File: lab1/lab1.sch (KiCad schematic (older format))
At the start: 15 parts

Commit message: Finish 1.8-1.10
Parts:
- added J?: Conn_01x06_Male, symbol Connector:Conn_01x06_Male
- added J?: USB_OTG, symbol Connector:USB_OTG
- added U?: LM1117ADJ, symbol lab1:LM1117ADJ
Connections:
- net +3V3: now also J?.1 (Pin_1)
- net GND: now also J?.3 (Pin_3), J?.5 (GND), J?.6 (Shield)
- new net: J?.1 (VBUS), U?.3 (Vin)
- new net NRST: J?.5 (Pin_5)
- new net PA13: J?.4 (Pin_4)
- new net PA14: J?.2 (Pin_2)
- new net PB3: J?.6 (Pin_6)
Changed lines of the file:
@@
 	4850 4400 4350 4400
 Connection ~ 4350 4400
+$Comp
+L Connector:Conn_01x06_Male J?
+U 1 1 5E299ECA
+P 8650 1750
+F 0 "J?" H 8758 2131 50  0000 C CNN
+F 1 "Conn_01x06_Male" H 8758 2040 50  0000 C CNN
+F 2 "" H 8650 1750 50  0001 C CNN
+F 3 "~" H 8650 1750 50  0001 C CNN
+	1    8650 1750
+	1    0    0    -1
+$EndComp
+Text Label 9500 1950 0    50   ~ 0
+NRST
+$Comp
+L power:+3.3V #PWR?
+U 1 1 5E29CFF8
+P 9500 1550
+F 0 "#PWR?" H 9500 1400 50  0001 C CNN
+F 1 "+3.3V" H 9515 1723 50  0000 C CNN
+F 2 "" H 9500 1550 50  0001 C CNN
+F 3 "" H 9500 1550 50  0001 C CNN
+	1    9500 1550
+	1    0    0    -1
+$EndComp
+Wire Wire Line
+	8850 1750 10400 1750
+$Comp
+L power:GND #PWR?
+U 1 1 5E29B658
+P 10400 1750
+F 0 "#PWR?" H 10400 1500 50  0001 C CNN
+F 1 "GND" H 10405 1577 50  0000 C CNN
+F 2 "" H 10400 1750 50  0001 C CNN
+F 3 "" H 10400 1750 50  0001 C CNN
+	1    10400 1750
+	1    0    0    -1
+$EndComp
+Wire Wire Line
+	8850 1550 9500 1550
+Text Label 9500 1650 0    50   ~ 0
+PA14
+Wire Wire Line
+	8850 1650 9500 1650
+Text Label 9500 1850 0    50   ~ 0
+PA13
+Wire Wire Line
+	8850 1850 9500 1850
+Wire Wire Line
+	8850 1950 9500 1950
+Text Label 9500 2050 0    50   ~ 0
+PB3
+Wire Wire Line
+	8850 2050 9500 2050
+$Comp
+L lab1:LM1117ADJ U?
+U 1 1 5E2BD33D
+P 9200 4200
+F 0 "U?" H 9200 4515 50  0000 C CNN
+F 1 "LM1117ADJ" H 9200 4424 50  0000 C CNN
+F 2 "" H 9300 3650 50  0001 C CNN
+F 3 "" H 9300 3650 50  0001 C CNN
+	1    9200 4200
+	1    0    0    -1
+$EndComp
+$Comp
+L Connector:USB_OTG J?
+U 1 1 5E2C2E5A
+P 7600 4350
+F 0 "J?" H 7657 4817 50  0000 C CNN
+F 1 "USB_OTG" H 7657 4726 50  0000 C CNN
+F 2 "" H 7750 4300 50  0001 C CNN
+F 3 " ~" H 7750 4300 50  0001 C CNN
+	1    7600 4350
+	1    0    0    -1
+$EndComp
+Wire Wire Line
+	7500 4750 7500 4850
+Wire Wire Line
+	7500 4850 7550 4850
+Wire Wire Line
+	7600 4850 7600 4750
+$Comp
+L power:GND #PWR?
+U 1 1 5E2C5ACE
+P 7550 4950
+F 0 "#PWR?" H 7550 4700 50  0001 C CNN
+F 1 "GND" H 7555 4777 50  0000 C CNN
+F 2 "" H 7550 4950 50  0001 C CNN
+F 3 "" H 7550 4950 50  0001 C CNN
+	1    7550 4950
+	1    0    0    -1
+$EndComp
+Wire Wire Line
+	7550 4950 7550 4850
+Connection ~ 7550 4850
+Wire Wire Line
+	7550 4850 7600 4850
+Wire Wire Line
+	7900 4150 8250 4150
+Wire Wire Line
+	8250 4150 8250 3650
+Wire Wire Line
+	8250 3650 9950 3650
+Wire Wire Line
+	9950 3650 9950 4150
+Wire Wire Line
+	9950 4150 9650 4150
 $EndSCHEMATC

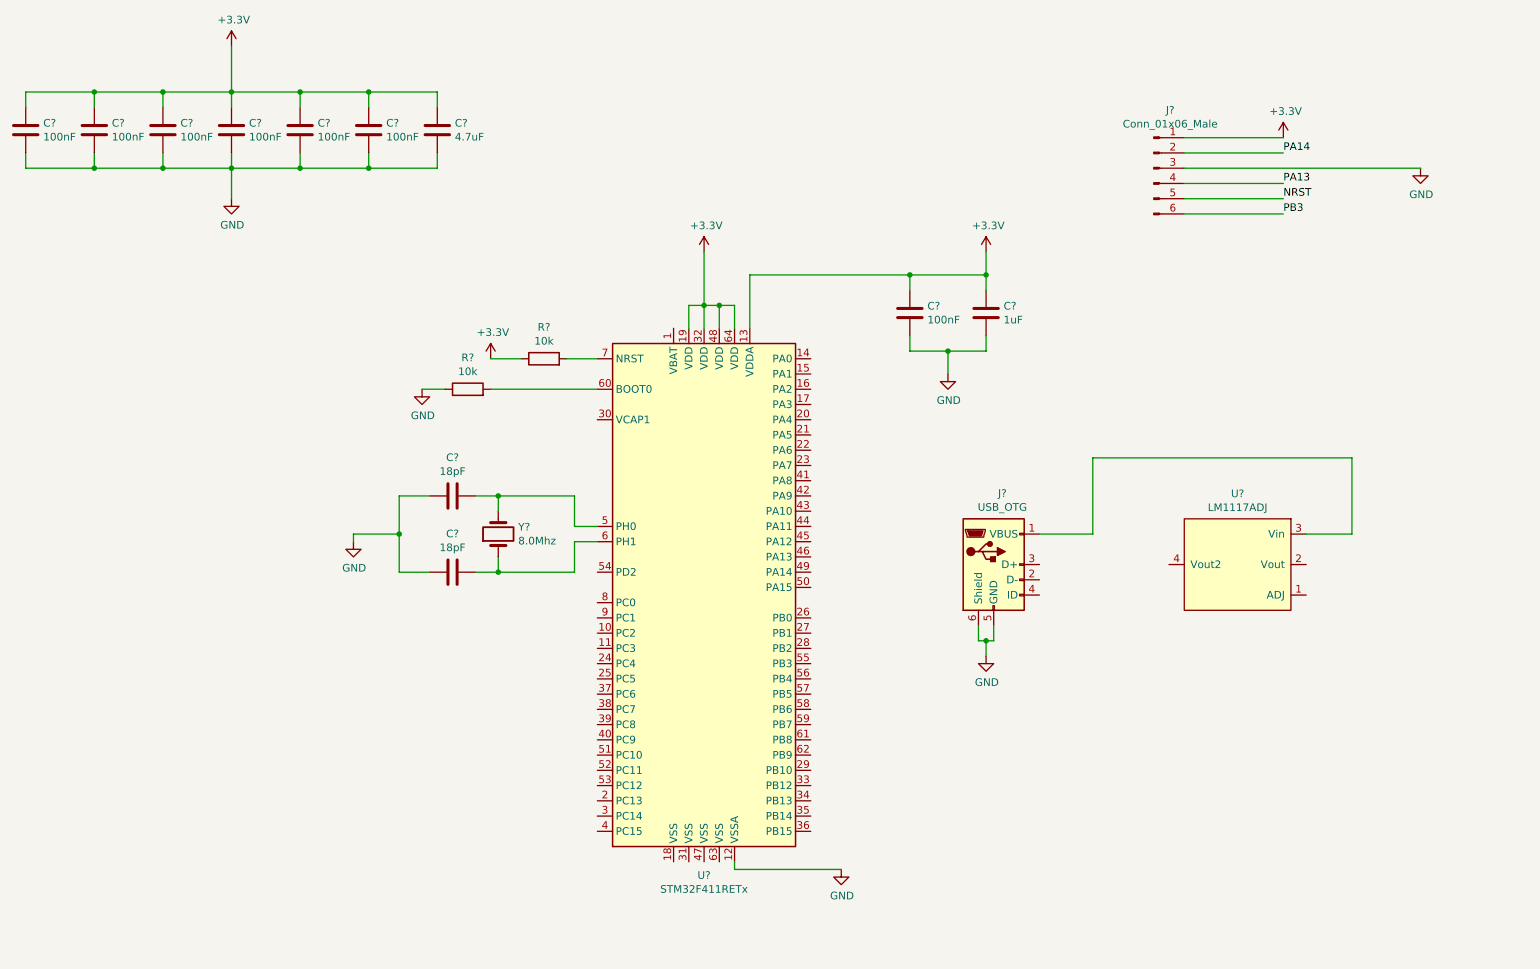
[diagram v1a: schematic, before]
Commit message: Add footprint to most components
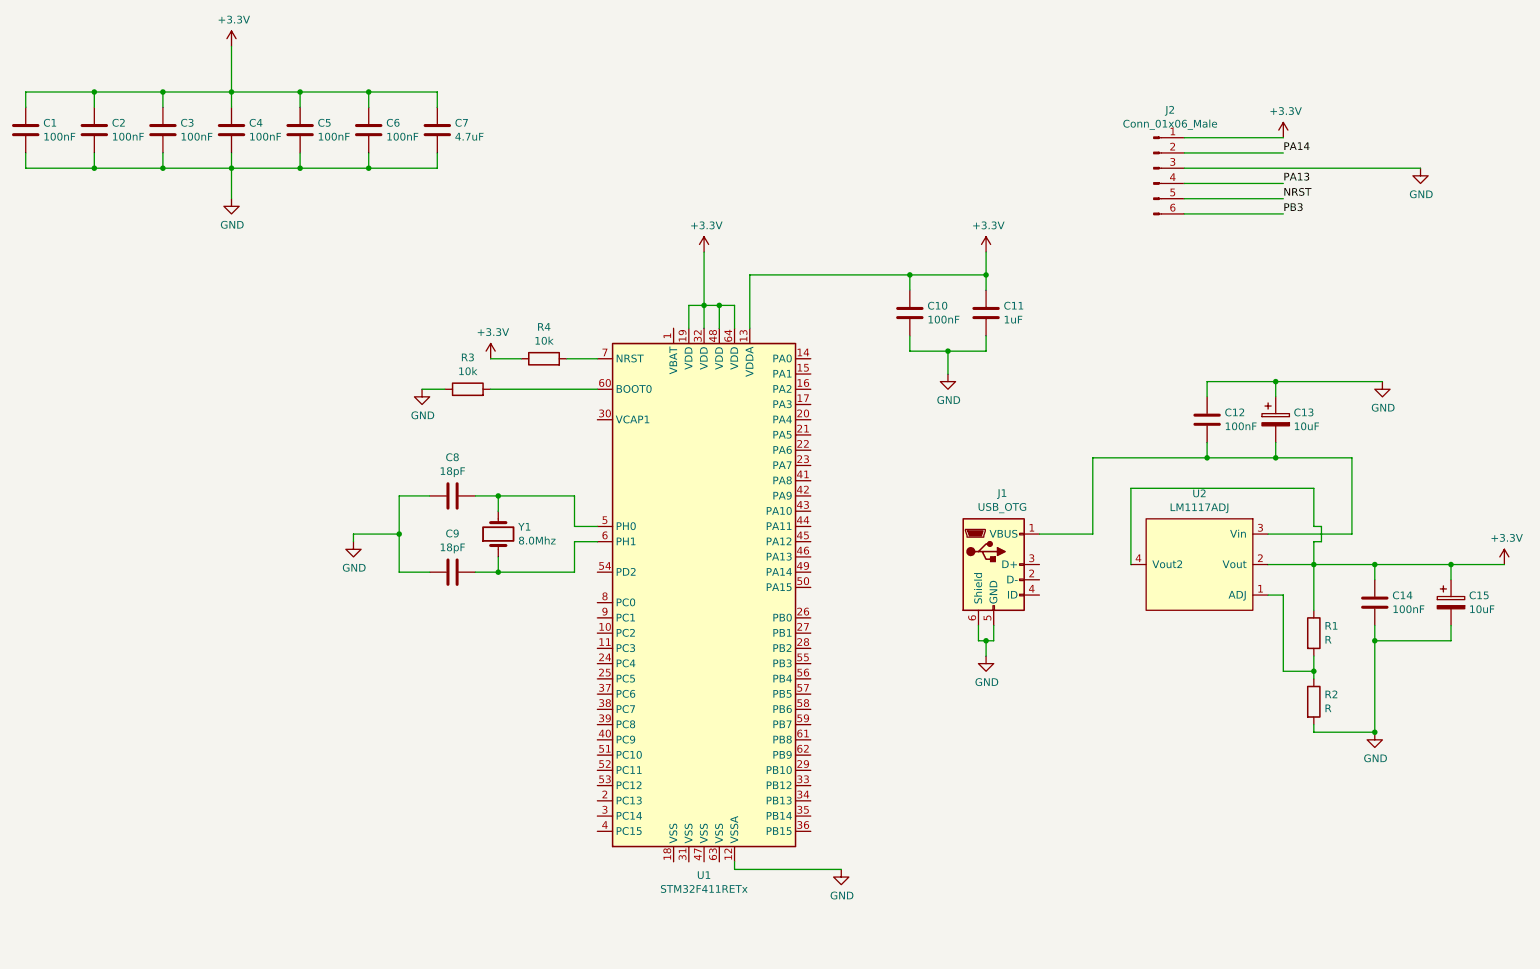
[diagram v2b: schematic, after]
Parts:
- added C12, C14: 100nF, Capacitor_SMD:C_0805_2012Metric_Pad1.15x1.40mm_HandSolder, symbol Device:C
- added C13, C15: 10uF, Capacitor_SMD:CP_Elec_4x4.5, symbol Device:CP
- added R1, R2: R, Resistor_SMD:R_0805_2012Metric_Pad1.15x1.40mm_HandSolder, symbol Device:R
- C1, C10, C11, C2, C3, C4, C5, C6, C7, C8, C9: renamed from C?; footprint (none) -> Capacitor_SMD:C_0805_2012Metric_Pad1.15x1.40mm_HandSolder
- J1: renamed from J?; footprint (none) -> Connector_USB:USB_Mini-B_AdamTech_MUSB-B5-S-VT-TSMT-1_SMD_Vertical
- R3, R4: renamed from R?; footprint (none) -> Resistor_SMD:R_0805_2012Metric_Pad1.15x1.40mm_HandSolder
- Y1: renamed from Y?; footprint (none) -> Crystal:Crystal_SMD_5032-4Pin_5.0x3.2mm
- gave numbers to parts that had none: 3
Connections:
- net +3V3: now also U2.2 (Vout), U2.4 (Vout2), C14.1, C15.1, R1.1
- net GND: now also C12.1, C13.1, C14.2, C15.2, R2.2
- net at U2.1 (ADJ): now also R1.2, R2.1
- net at J1.1 (VBUS), U2.3 (Vin): now also C12.2, C13.2
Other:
- moved on the sheet: U2

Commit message: Finish lab 1
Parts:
- added C16: 4.7uF, Capacitor_SMD:C_0805_2012Metric_Pad1.15x1.40mm_HandSolder, symbol Device:C
- J2: footprint (none) -> Connector_PinHeader_2.54mm:PinHeader_1x06_P2.54mm_Vertical
- U2: footprint (none) -> Package_TO_SOT_SMD:SOT-223
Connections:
- net PA13 is gone; now on net SWDIO: J2.4 (Pin_4)
- net PA14 is gone; now on net SWCLK: J2.2 (Pin_2)
- net PB3 is gone; now on net SWO: J2.6 (Pin_6)
- net +3V3: now also U1.1 (VBAT); no longer U2.4 (Vout2)
- net GND: now also U1.18 (VSS), U1.31 (VSS), U1.47 (VSS), U1.63 (VSS), C16.2
- net NRST: now also R4.2, U1.7 (NRST)
- net at U1.30 (VCAP1): now also C16.1
- net SWDIO: now reaches U1.46 (PA13)
- net SWCLK: now reaches U1.49 (PA14)
- net SWO: now reaches U1.55 (PB3)
- net +5V: now reaches C12.2, C13.2, J1.1 (VBUS), U2.3 (Vin)
- no-connect marks 0 -> 49
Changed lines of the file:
@@
 	5700 2650 5700 2300
-$Comp
-L power:GND #PWR0106
-U 1 1 5E2C43EA
-P 6600 6350
-F 0 "#PWR0106" H 6600 6100 50  0001 C CNN
-F 1 "GND" H 6605 6177 50  0000 C CNN
-F 2 "" H 6600 6350 50  0001 C CNN
-F 3 "" H 6600 6350 50  0001 C CNN
-	1    6600 6350
-	1    0    0    -1
-$EndComp
-Wire Wire Line
-	5900 6300 5900 6350
-Wire Wire Line
-	5900 6350 6600 6350
 $Comp
 L Device:R R4
@@
 F 0 "J2" H 8758 2131 50  0000 C CNN
 F 1 "Conn_01x06_Male" H 8758 2040 50  0000 C CNN
-F 2 "" H 8650 1750 50  0001 C CNN
+F 2 "Connector_PinHeader_2.54mm:PinHeader_1x06_P2.54mm_Vertical" H 8650 1750 50  0001 C CNN
 F 3 "~" H 8650 1750 50  0001 C CNN
 	1    8650 1750
@@
 	8850 1550 9500 1550
 Text Label 9500 1650 0    50   ~ 0
-PA14
+SWCLK
 Wire Wire Line
 	8850 1650 9500 1650
 Text Label 9500 1850 0    50   ~ 0
-PA13
+SWDIO
 Wire Wire Line
 	8850 1850 9500 1850
@@
 	8850 1950 9500 1950
 Text Label 9500 2050 0    50   ~ 0
-PB3
+SWO
 Wire Wire Line
 	8850 2050 9500 2050
-$Comp
-L lab1:LM1117ADJ U2
-U 1 1 5E2BD33D
-P 8950 4200
-F 0 "U2" H 8950 4515 50  0000 C CNN
-F 1 "LM1117ADJ" H 8950 4424 50  0000 C CNN
-F 2 "" H 9050 3650 50  0001 C CNN
-F 3 "" H 9050 3650 50  0001 C CNN
-	1    8950 4200
-	1    0    0    -1
-$EndComp
 $Comp
 L Connector:USB_OTG J1
@@
 Wire Wire Line
 	9450 3650 9950 3650
-Wire Wire Line
-	8500 3850 9700 3850
-Wire Wire Line
-	9700 3850 9700 4100
-Wire Wire Line
-	9700 4100 9750 4100
-Wire Wire Line
-	9750 4100 9750 4200
-Wire Wire Line
-	9750 4200 9700 4200
-Wire Wire Line
-	9700 4200 9700 4350
-Wire Wire Line
-	8500 3850 8500 4350
+$Comp
+L power:+5V #PWR0116
+U 1 1 5E2AF00A
+P 8250 3600
+F 0 "#PWR0116" H 8250 3450 50  0001 C CNN
+F 1 "+5V" H 8265 3773 50  0000 C CNN
+F 2 "" H 8250 3600 50  0001 C CNN
+F 3 "" H 8250 3600 50  0001 C CNN
+	1    8250 3600
+	1    0    0    -1
+$EndComp
+Wire Wire Line
+	8250 3600 8250 3650
+Connection ~ 8250 3650
+Text Label 6400 4300 0    50   ~ 0
+SWDIO
+Text Label 6400 4400 0    50   ~ 0
+SWCLK
+Text Label 6400 5000 0    50   ~ 0
+SWO
+NoConn ~ 5000 4400
+NoConn ~ 5000 4600
+NoConn ~ 5000 4700
+NoConn ~ 5000 4800
+NoConn ~ 5000 4900
+NoConn ~ 5000 5000
+NoConn ~ 5000 5100
+NoConn ~ 5000 5200
+NoConn ~ 5000 5300
+NoConn ~ 5000 5400
+NoConn ~ 5000 5500
+NoConn ~ 5000 5600
+NoConn ~ 5000 5700
+NoConn ~ 5000 5800
+NoConn ~ 5000 5900
+NoConn ~ 5000 6000
+NoConn ~ 5000 6100
+NoConn ~ 6400 3000
+NoConn ~ 6400 3100
+NoConn ~ 6400 3200
+NoConn ~ 6400 3300
+NoConn ~ 6400 3400
+NoConn ~ 6400 3500
+NoConn ~ 6400 3600
+NoConn ~ 6400 3700
+NoConn ~ 6400 3800
+NoConn ~ 6400 3900
+NoConn ~ 6400 4000
+NoConn ~ 6400 4100
+NoConn ~ 6400 4200
+NoConn ~ 6400 4500
+NoConn ~ 6400 4700
+NoConn ~ 6400 4800
+NoConn ~ 6400 4900
+NoConn ~ 6400 5100
+NoConn ~ 6400 5200
+NoConn ~ 6400 5300
+NoConn ~ 6400 5400
+NoConn ~ 6400 5500
+NoConn ~ 6400 5600
+NoConn ~ 6400 5700
+NoConn ~ 6400 5800
+NoConn ~ 6400 6100
+NoConn ~ 6400 5900
+NoConn ~ 6400 6000
+NoConn ~ 7900 4350
+NoConn ~ 7900 4450
+NoConn ~ 7900 4550
+$Comp
+L lab1:LM1117ADJ U2
+U 1 1 5E2BD33D
+P 8950 4200
+F 0 "U2" H 8950 4515 50  0000 C CNN
+F 1 "LM1117ADJ" H 8950 4424 50  0000 C CNN
+F 2 "Package_TO_SOT_SMD:SOT-223" H 9050 3650 50  0001 C CNN
+F 3 "" H 9050 3650 50  0001 C CNN
+	1    8950 4200
+	1    0    0    -1
+$EndComp
+$Comp
+L power:GND #PWR0106
+U 1 1 5E397CA6
+P 5700 6700
+F 0 "#PWR0106" H 5700 6450 50  0001 C CNN
+F 1 "GND" H 5705 6527 50  0000 C CNN
+F 2 "" H 5700 6700 50  0001 C CNN
+F 3 "" H 5700 6700 50  0001 C CNN
+	1    5700 6700
+	1    0    0    -1
+$EndComp
+Wire Wire Line
+	5800 6300 5800 6600
+Wire Wire Line
+	5800 6600 5700 6600
+Wire Wire Line
+	5500 6600 5500 6300
+Wire Wire Line
+	5600 6300 5600 6600
+Connection ~ 5600 6600
+Wire Wire Line
+	5600 6600 5500 6600
+Wire Wire Line
+	5700 6300 5700 6600
+Connection ~ 5700 6600
+Wire Wire Line
+	5700 6600 5600 6600
+Wire Wire Line
+	5800 6600 5900 6600
+Connection ~ 5800 6600
+Wire Wire Line
+	5700 6600 5700 6700
+Wire Wire Line
+	5900 6300 5900 6600
+Wire Wire Line
+	5500 2800 5500 2650
+Wire Wire Line
+	5500 2650 5600 2650
+Connection ~ 5600 2650
+NoConn ~ 8500 4350
+$Comp
+L Device:C C16
+U 1 1 5E2B322F
+P 3400 3400
+F 0 "C16" V 3148 3400 50  0000 C CNN
+F 1 "4.7uF" V 3239 3400 50  0000 C CNN
+F 2 "Capacitor_SMD:C_0805_2012Metric_Pad1.15x1.40mm_HandSolder" H 3438 3250 50  0001 C CNN
+F 3 "~" H 3400 3400 50  0001 C CNN
+	1    3400 3400
+	0    1    1    0
+$EndComp
+Wire Wire Line
+	5000 3400 3550 3400
+$Comp
+L power:GND #PWR0117
+U 1 1 5E2C2467
+P 3100 3550
+F 0 "#PWR0117" H 3100 3300 50  0001 C CNN
+F 1 "GND" H 3105 3377 50  0000 C CNN
+F 2 "" H 3100 3550 50  0001 C CNN
+F 3 "" H 3100 3550 50  0001 C CNN
+	1    3100 3550
+	1    0    0    -1
+$EndComp
+Wire Wire Line
+	3250 3400 3100 3400
+Wire Wire Line
+	3100 3400 3100 3550
+Text Label 4800 3000 0    50   ~ 0
+NRST
 $EndSCHEMATC

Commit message: Finish lab 1 for real
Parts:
- J1: footprint Connector_USB:USB_Mini-B_AdamTech_MUSB-B5-S-VT-TSMT-1_SMD_Vertical -> Connector_USB:USB_Mini-B_Lumberg_2486_01_Horizontal
- R1: value R -> 2k
- R2: value R -> 1k
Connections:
- net +3V3: now also U2.4 (Vout2)
- net +5V: now also C13.1; no longer C13.2
- net GND: now also C13.2; no longer C13.1
- no-connect marks 49 -> 48
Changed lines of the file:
@@
 F 0 "J1" H 7657 4817 50  0000 C CNN
 F 1 "USB_OTG" H 7657 4726 50  0000 C CNN
-F 2 "Connector_USB:USB_Mini-B_AdamTech_MUSB-B5-S-VT-TSMT-1_SMD_Vertical" H 7750 4300 50  0001 C CNN
+F 2 "Connector_USB:USB_Mini-B_Lumberg_2486_01_Horizontal" H 7750 4300 50  0001 C CNN
 F 3 " ~" H 7750 4300 50  0001 C CNN
 	1    7600 4350
@@
 U 1 1 5E2ACF21
 P 9450 3400
-F 0 "C13" H 9568 3446 50  0000 L CNN
-F 1 "10uF" H 9568 3355 50  0000 L CNN
+F 0 "C13" H 9332 3354 50  0000 R CNN
+F 1 "10uF" H 9332 3445 50  0000 R CNN
 F 2 "Capacitor_SMD:CP_Elec_4x4.5" H 9488 3250 50  0001 C CNN
 F 3 "~" H 9450 3400 50  0001 C CNN
 	1    9450 3400
-	1    0    0    -1
+	-1   0    0    1
 $EndComp
 $Comp
@@
 	1    0    0    -1
 $EndComp
-$Comp
-L Device:CP C15
-U 1 1 5E2E66BE
-P 10600 4600
-F 0 "C15" H 10718 4646 50  0000 L CNN
-F 1 "10uF" H 10718 4555 50  0000 L CNN
-F 2 "Capacitor_SMD:CP_Elec_4x4.5" H 10638 4450 50  0001 C CNN
-F 3 "~" H 10600 4600 50  0001 C CNN
-	1    10600 4600
-	1    0    0    -1
-$EndComp
 Wire Wire Line
 	8250 3650 9000 3650
@@
 P 9700 4800
 F 0 "R1" H 9770 4846 50  0000 L CNN
-F 1 "R" H 9770 4755 50  0000 L CNN
+F 1 "2k" H 9770 4755 50  0000 L CNN
 F 2 "Resistor_SMD:R_0805_2012Metric_Pad1.15x1.40mm_HandSolder" V 9630 4800 50  0001 C CNN
 F 3 "~" H 9700 4800 50  0001 C CNN
@@
 P 9700 5250
 F 0 "R2" H 9770 5296 50  0000 L CNN
-F 1 "R" H 9770 5205 50  0000 L CNN
+F 1 "1k" H 9770 5205 50  0000 L CNN
 F 2 "Resistor_SMD:R_0805_2012Metric_Pad1.15x1.40mm_HandSolder" V 9630 5250 50  0001 C CNN
 F 3 "~" H 9700 5250 50  0001 C CNN
@@
 Wire Wire Line
 	9400 4150 9950 4150
-Wire Wire Line
-	9400 4350 9700 4350
 Connection ~ 10100 4350
 Wire Wire Line
@@
 	5500 2650 5600 2650
 Connection ~ 5600 2650
-NoConn ~ 8500 4350
 $Comp
 L Device:C C16
@@
 Text Label 4800 3000 0    50   ~ 0
 NRST
+$Comp
+L Device:CP C15
+U 1 1 5E2E66BE
+P 10600 4600
+F 0 "C15" H 10718 4646 50  0000 L CNN
+F 1 "10uF" H 10718 4555 50  0000 L CNN
+F 2 "Capacitor_SMD:CP_Elec_4x4.5" H 10638 4450 50  0001 C CNN
+F 3 "~" H 10600 4600 50  0001 C CNN
+	1    10600 4600
+	1    0    0    -1
+$EndComp
+Wire Wire Line
+	8500 4350 8450 4350
+Wire Wire Line
+	8450 4350 8450 3850
+Wire Wire Line
+	8450 3850 9700 3850
+Wire Wire Line
+	9700 3850 9700 4350
+Wire Wire Line
+	9400 4350 9700 4350
 $EndSCHEMATC
